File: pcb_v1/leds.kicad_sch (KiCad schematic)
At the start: 132 parts

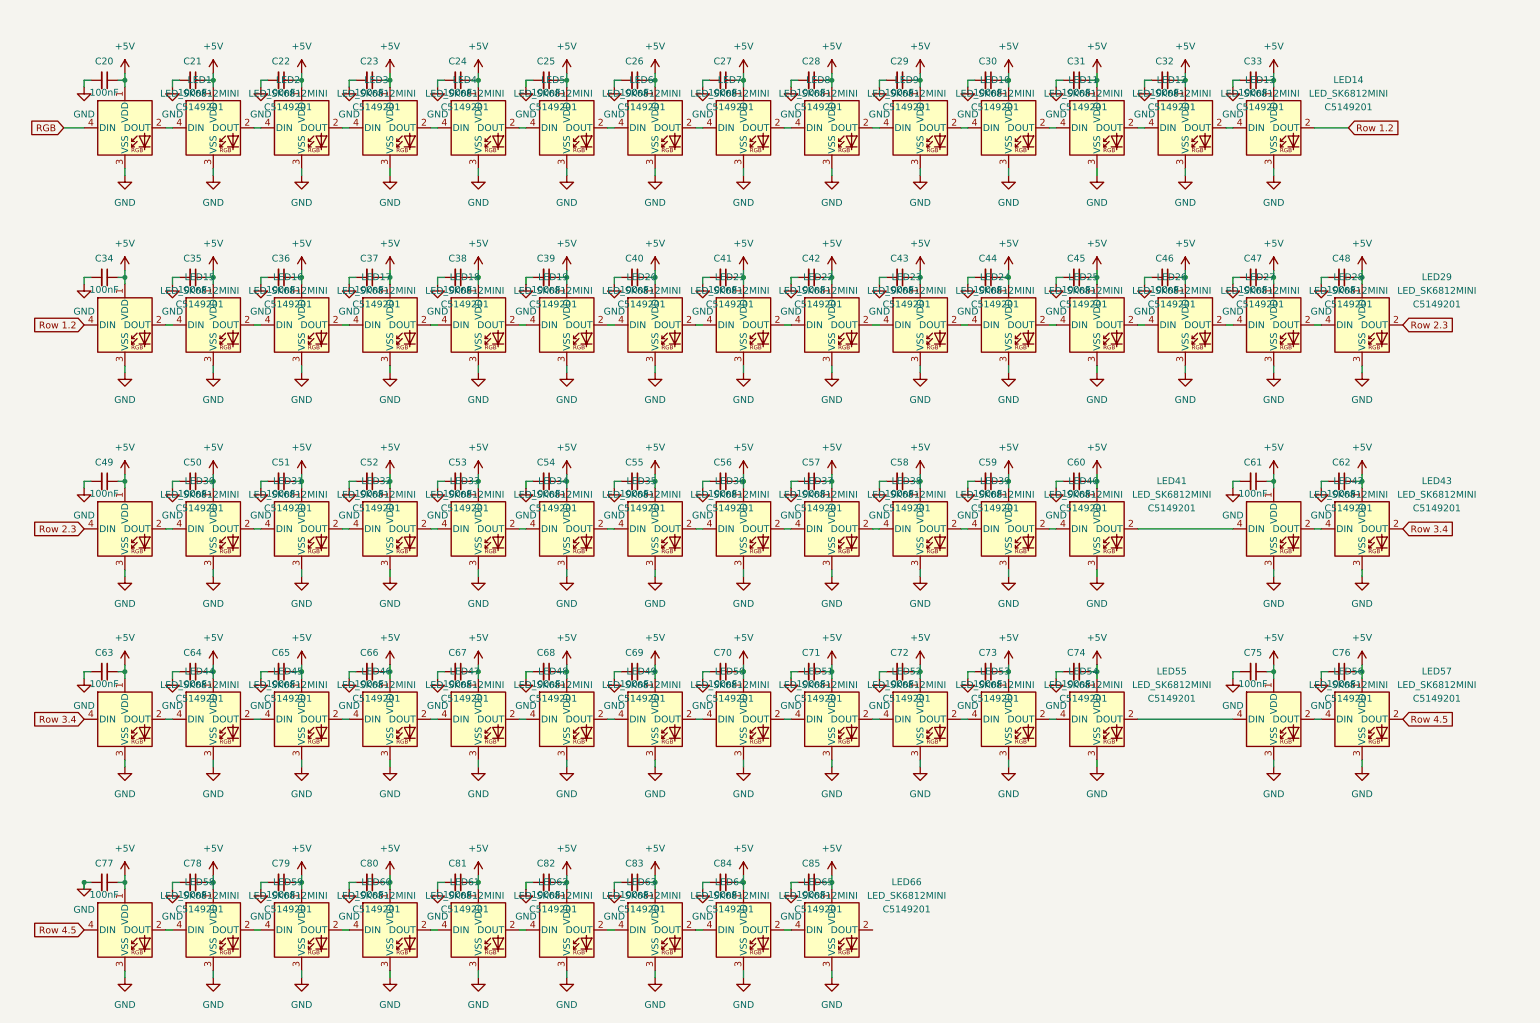
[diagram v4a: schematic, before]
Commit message: Connected all switches, LEDs to MCU
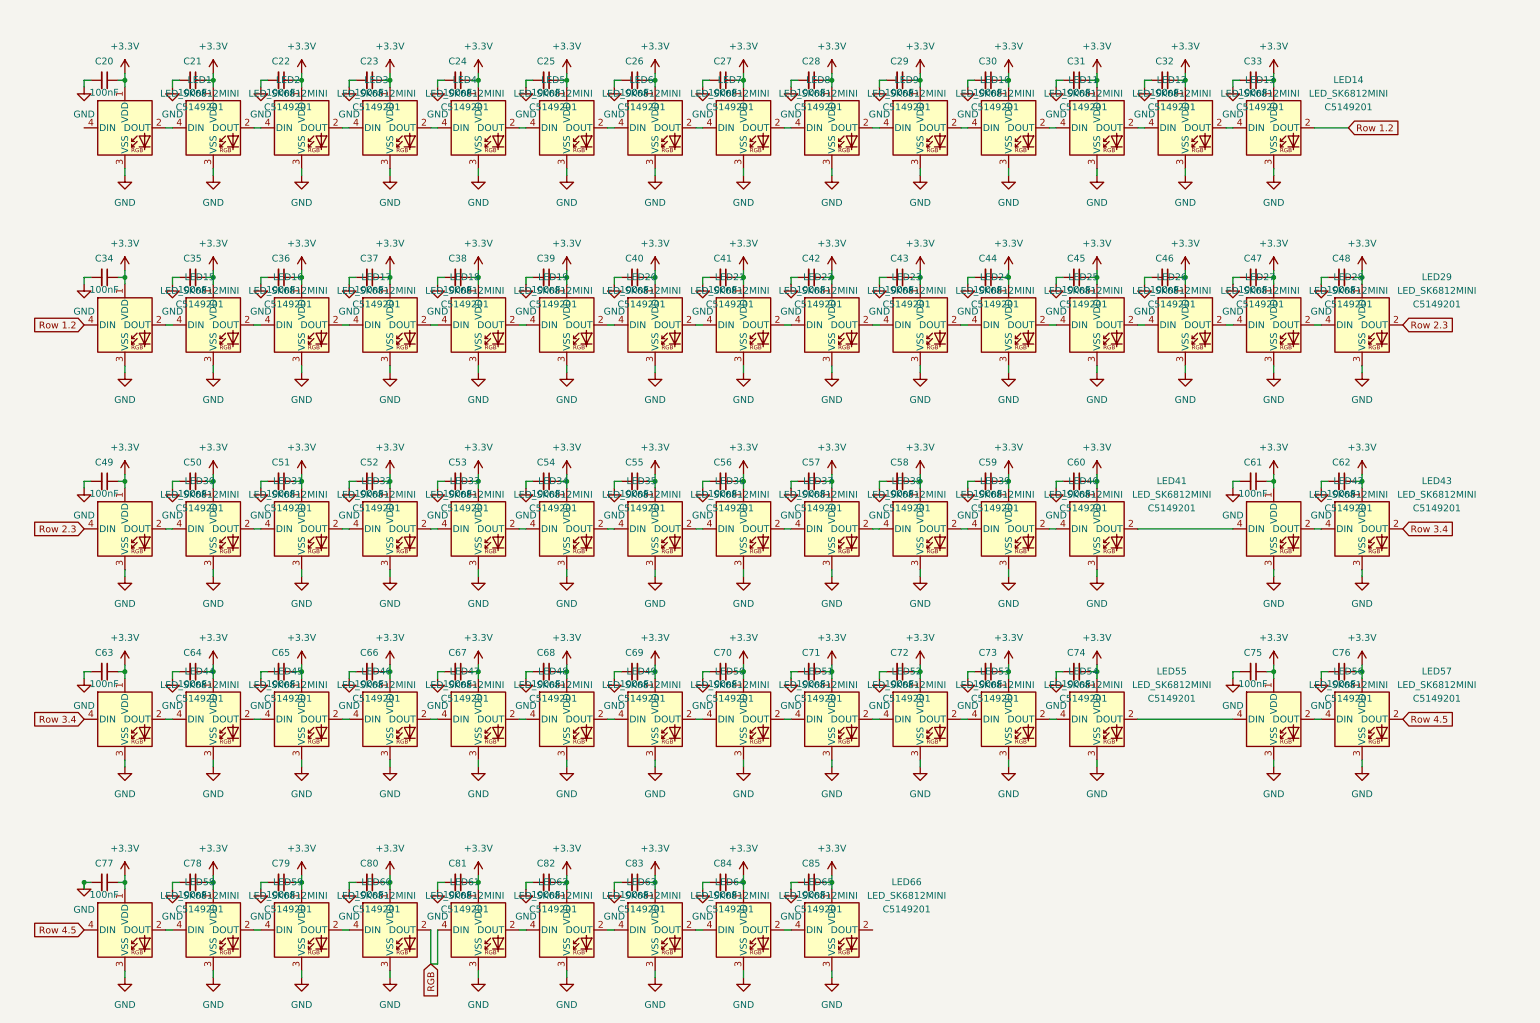
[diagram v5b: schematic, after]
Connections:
- net RGB: now also LED61.2 (DOUT), LED62.4 (DIN); no longer LED1.4 (DIN)
- net +5V renamed +3.3V

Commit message: Updated wiring
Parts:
- C20, C21, C22, C23, C24, C25, C26, C27, C28, C29, C30, C31, C32, C33, C34, C35, C36, C37, C38, C39, C40, C41, C42, C43, C44, C45, C46, C47, C48, C49, C50, C51, C52, C53, C54, C55, C56, C57, C58, C59, C60, C61, C62, C63, C64, C65, C66, C67, C68, C69, C70, C71, C72, C73, C74, C75, C76, C77, C78, C79, C80, C81, C82, C83, C84, C85: footprint Capacitor_SMD:C_0805_2012Metric -> Murata Capacitor:CAPC1608X90N

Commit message: Wired all keyboard matrix pins
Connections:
- net RGB: now also LED60.2 (DOUT), LED61.4 (DIN); no longer LED61.2 (DOUT), LED62.4 (DIN)
- new net: LED61.2 (DOUT), LED62.4 (DIN)
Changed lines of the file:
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@@
 	(wire
 		(pts
-			(xy 71.12 186.69) (xy 72.39 186.69)
+			(xy 71.12 191.77) (xy 72.39 191.77)
 		)
 		(stroke
@@
 	(wire
 		(pts
-			(xy 88.9 193.04) (xy 88.9 186.69)
+			(xy 212.09 26.67) (xy 212.09 27.94)
 		)
 		(stroke
@@
 	(wire
 		(pts
-			(xy 212.09 26.67) (xy 212.09 27.94)
+			(xy 55.88 138.43) (xy 55.88 139.7)
 		)
 		(stroke
@@
 	(wire
 		(pts
-			(xy 55.88 138.43) (xy 55.88 139.7)
+			(xy 71.12 191.77) (xy 71.12 186.69)
 		)
 		(stroke
@@
 	(wire
 		(pts
+			(xy 72.39 191.77) (xy 72.39 186.69)
+		)
+		(stroke
+			(width 0)
+			(type default)
+		)
+	)
+	(wire
+		(pts
 			(xy 62.23 102.87) (xy 63.5 102.87)
 		)
@@
 	(wire
 		(pts
-			(xy 254 102.87) (xy 254 104.14)
+			(xy 88.9 186.69) (xy 87.63 186.69)
 		)
 		(stroke
@@
 	(wire
 		(pts
-			(xy 73.66 138.43) (xy 72.39 138.43)
+			(xy 254 102.87) (xy 254 104.14)
 		)
 		(stroke
@@
 	(wire
 		(pts
-			(xy 222.25 27.94) (xy 220.98 27.94)
+			(xy 73.66 138.43) (xy 72.39 138.43)
 		)
 		(stroke
@@
 	(wire
 		(pts
-			(xy 238.76 102.87) (xy 237.49 102.87)
+			(xy 222.25 27.94) (xy 220.98 27.94)
 		)
 		(stroke
@@
 	(wire
 		(pts
-			(xy 87.63 193.04) (xy 88.9 193.04)
+			(xy 238.76 102.87) (xy 237.49 102.87)
 		)
 		(stroke
@@
 	(wire
 		(pts
-			(xy 87.63 193.04) (xy 87.63 186.69)
-		)
-		(stroke
-			(width 0)
-			(type default)
-		)
-	)
-	(wire
-		(pts
 			(xy 24.13 102.87) (xy 22.86 102.87)
 		)
@@
 		)
 	)
-	(global_label "Row 2.3"
+	(global_label "RGB"
 		(shape input)
-		(at 269.24 73.66 0)
+		(at 72.39 191.77 270)
 		(fields_autoplaced yes)
 		(effects
@@
 				(size 1.27 1.27)
 			)
-			(justify left)
+			(justify right)
 		)
 		(property "Intersheetrefs" "${INTERSHEET_REFS}"
-			(at 279.9661 73.66 0)
+			(at 72.39 198.5652 90)
 			(effects
 				(font
 					(size 1.27 1.27)
 				)
-				(justify left)
+				(justify right)
 				(hide yes)
 			)
 		)
 	)
-	(global_label "RGB"
+	(global_label "Row 2.3"
 		(shape input)
-		(at 87.63 193.04 270)
+		(at 269.24 73.66 0)
 		(fields_autoplaced yes)
 		(effects
@@
 				(size 1.27 1.27)
 			)
-			(justify right)
+			(justify left)
 		)
 		(property "Intersheetrefs" "${INTERSHEET_REFS}"
-			(at 87.63 199.8352 90)
+			(at 279.9661 73.66 0)
 			(effects
 				(font
 					(size 1.27 1.27)
 				)
-				(justify right)
+				(justify left)
 				(hide yes)
 			)

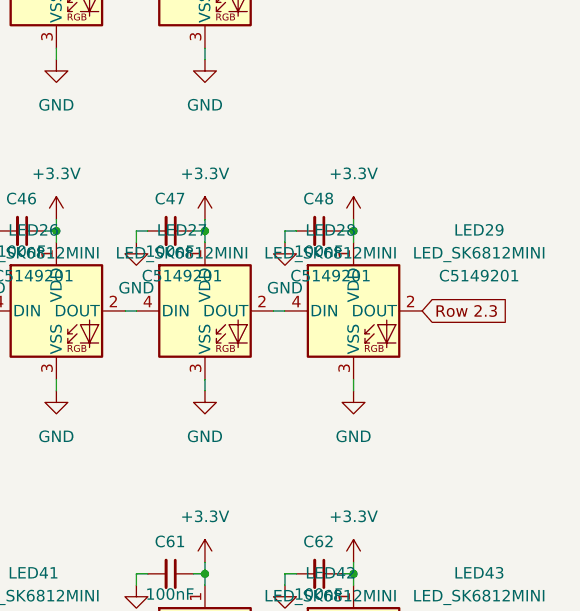
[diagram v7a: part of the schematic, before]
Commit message: Changed Layout of Keyboard
Row 1, Column 14 Removed due to OLED Screen taking up 2x2 u space
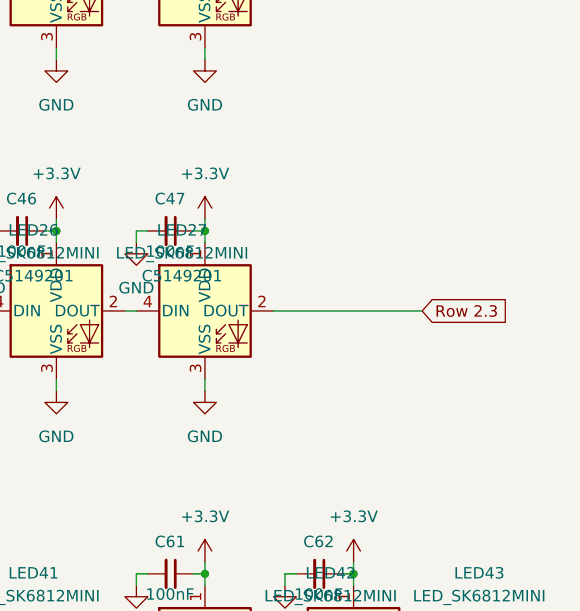
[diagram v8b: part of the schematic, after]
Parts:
- removed C48: 100nF, Murata Capacitor:CAPC1608X90N, symbol Device:C_Small
- removed LED29: LED_SK6812MINI, ScottoKeebs_Components:LED_SK6812MINI, symbol ScottoKeebs:LED_SK6812MINI
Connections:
- net Row 2.3: now also LED28.2 (DOUT)
